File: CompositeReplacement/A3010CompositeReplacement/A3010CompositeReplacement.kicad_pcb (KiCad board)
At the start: 2 copper layers, 35.7 x 70.1 mm, 25 parts, among them J3 Conn_Coaxial, U1 AD725, U2 Analog Video breakout, X1 17.734475MHZ

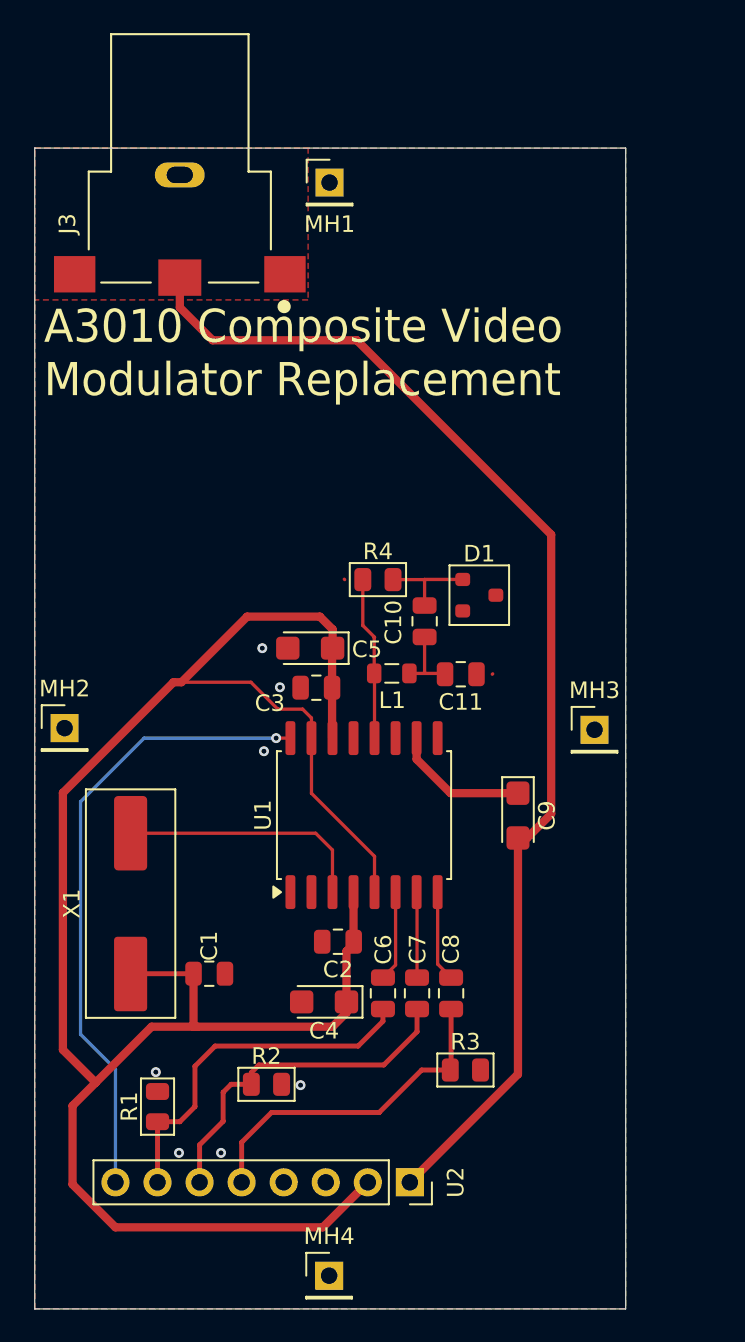
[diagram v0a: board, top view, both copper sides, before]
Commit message: fix power and cmposite output
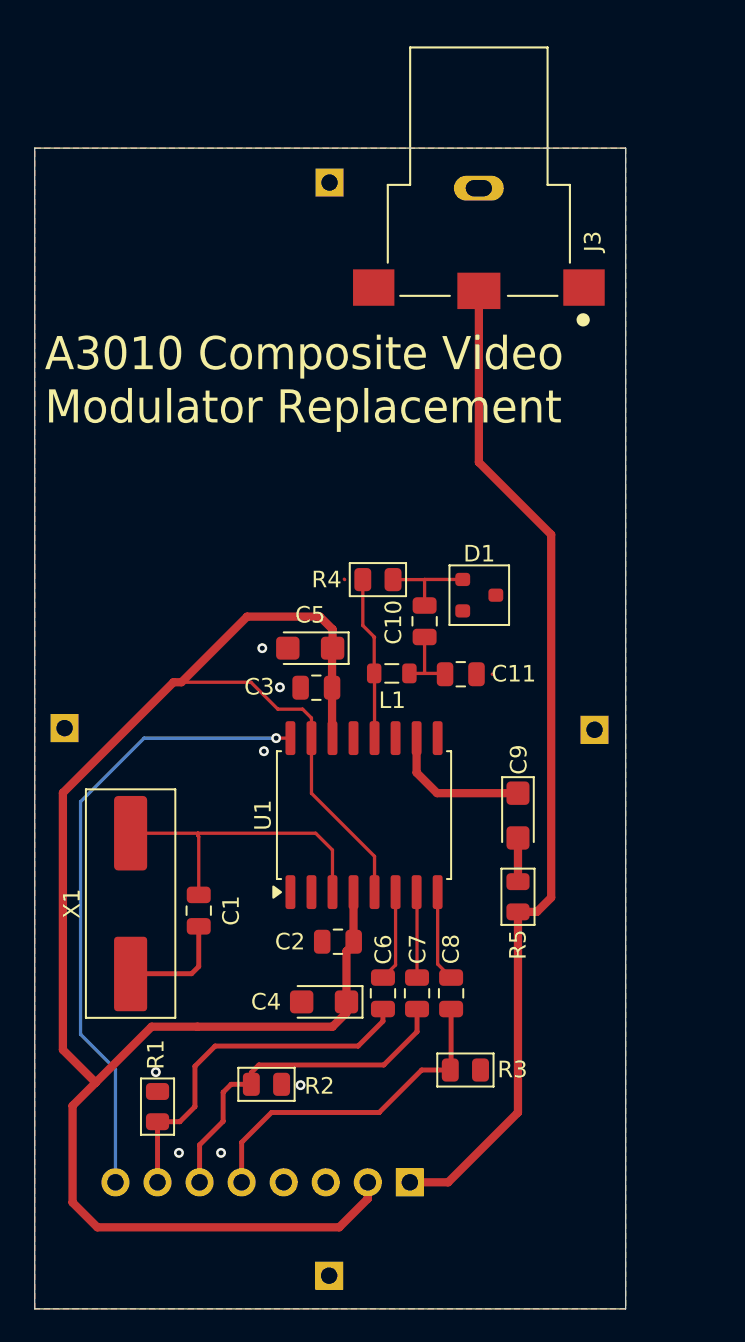
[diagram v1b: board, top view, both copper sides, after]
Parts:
- added R5: 75R, PCM_Resistor_SMD_AKL:R_0805_2012Metric, F.Cu at (128.0, 95.7)
- C1: value 100nF -> 10Pf
- MH1, MH2, MH3, MH4: moved to B.Cu
- U2: footprint Connector_PinSocket_2.54mm:PinSocket_1x08_P2.54mm_Vertical -> Connector_PinHeader_2.54mm:PinHeader_1x08_P2.54mm_Vertical; moved to B.Cu
- moved J3 18.1 mm to (125.7, 51.9)
- moved C1 3.86 mm to (108.8, 96.5), turned to -90 degrees
- turned MH1 to 180 degrees
- turned MH2 to 180 degrees
- turned MH3 to 180 degrees
- turned MH4 to 180 degrees
- turned U2 to 90 degrees
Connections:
- C1 pad 1: +5V -> Net-(U1-4FSC_CLK)
- C9 pad 2: /COMPout -> Net-(C9-Pad2)
- X1 pad 1: +5V -> GND
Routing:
- net /COMPout: track 72.9 -> 61.2 mm
- net GND: track 9.96 -> 16.7 mm
- net +5V: track 124.9 -> 119.1 mm
- net Net-(U1-4FSC_CLK): track 15.2 -> 18.9 mm
- net Net-(C9-Pad2): track 0.00 -> 2.64 mm
